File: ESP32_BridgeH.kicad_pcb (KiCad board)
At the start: 2 copper layers, 84.2 x 43.9 mm, 25 parts, among them J1 MT1, J2 MT2, J3 boot, J4 Serial, SW1 reset, U1 TB6612FNG, U2 ESP32-WROOM, U3 MPU6050, U4 LM7805_TO220

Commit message: Lodo added v2.0
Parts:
- added G***: LOGO, JuanDa_Lib:logoWolf, B.Cu at (188.9, 111.3)
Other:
- board text added: "ESP32 Wrober H-Bridge MPU6050 Serial Comunication"

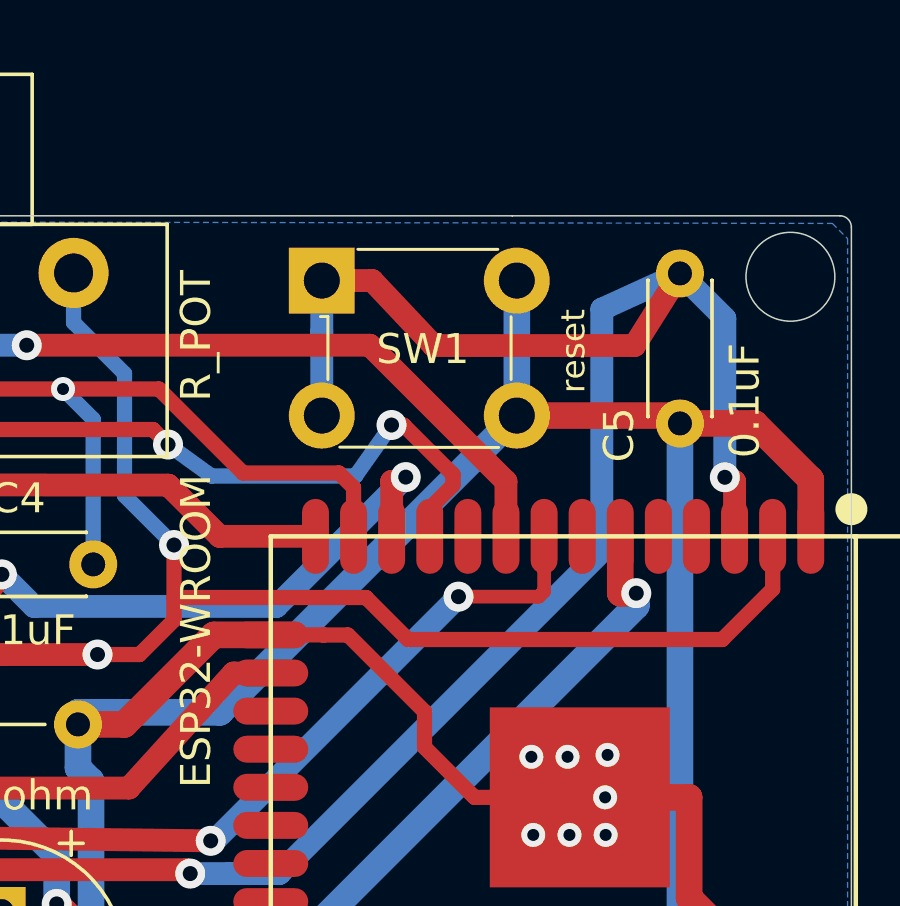
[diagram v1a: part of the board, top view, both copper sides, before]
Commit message: fix button problem
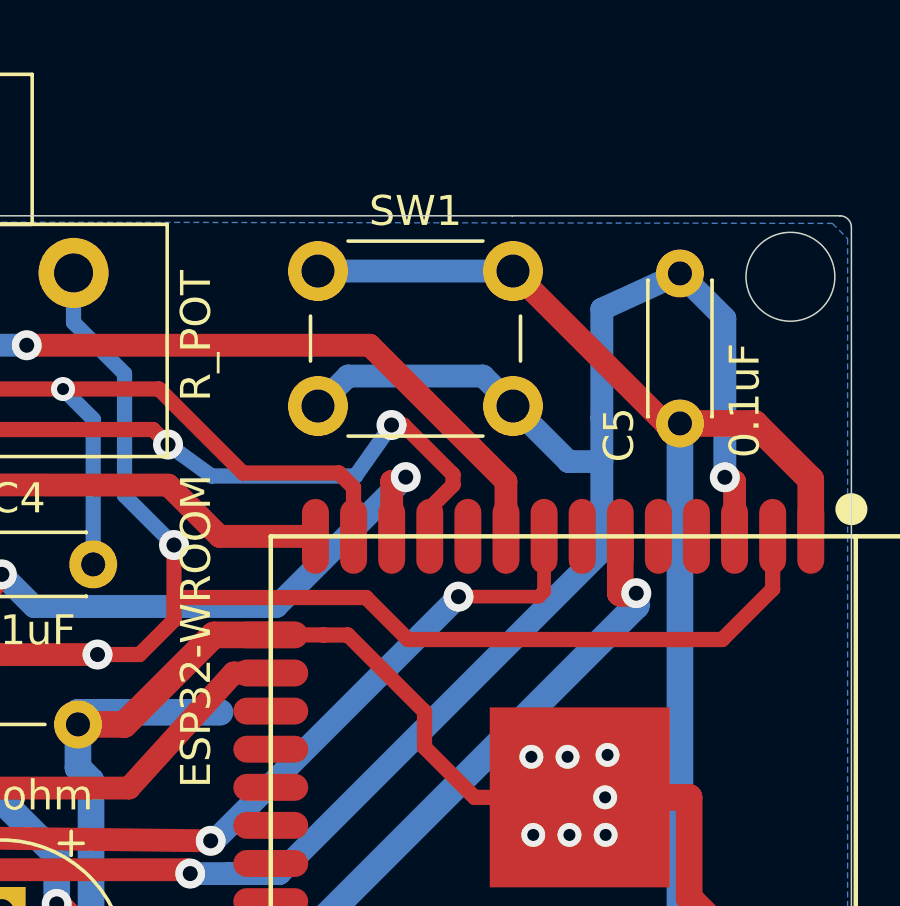
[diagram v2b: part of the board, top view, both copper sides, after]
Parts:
- SW1: value reset -> Reset; footprint digikey-footprints:Switch_Tactile_THT_6x6mm -> Button_Switch_THT:SW_PUSH_6mm
- moved SW1 0.34 mm to (188.8, 95.6)
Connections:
- SW1 pad 1: /reset -> GND
- SW1 pad 2: GND -> /reset
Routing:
- net GND: track 174.5 -> 164.6 mm
- net /reset: track 94.3 -> 86.7 mm
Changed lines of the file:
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@@
   )
   (setup
-    (last_trace_width 0.25)
+    (last_trace_width 0.762)
     (user_trace_width 0.508)
     (user_trace_width 0.762)
@@
     )
   )
-  (module digikey-footprints:Switch_Tactile_THT_6x6mm (layer F.Cu)
-    (at 188.976 95.885)
-    (descr http://www.te.com/commerce/DocumentDelivery/DDEController?Action=srchrtrv&DocNm=1825910&DocType=Customer+Drawing&DocLang=English)
-    (fp_text reference SW1 (at 3.3655 2.286 180) (layer F.SilkS)
-      (effects (font (size 1 1) (thickness 0.15)))
-    )
-    (fp_text value reset (at 8.382 2.3495 90) (layer F.SilkS)
-      (effects (font (size 0.8 0.8) (thickness 0.15)))
-    )
-    (fp_line (start 0.2032 1.2004) (end -0.0468 1.2004) (layer F.SilkS) (width 0.1))
-    (fp_line (start 5.8928 5.5626) (end 0.6 5.5528) (layer F.SilkS) (width 0.1))
-    (fp_line (start 6.3092 1.2048) (end 6.3092 3.3) (layer F.SilkS) (width 0.1))
-    (fp_line (start 0.2032 1.1938) (end 0.2032 3.302) (layer F.SilkS) (width 0.1))
-    (fp_line (start 1.2 -1.0414) (end 5.8674 -1.0414) (layer F.SilkS) (width 0.1))
-    (fp_line (start -1.35 -1.35) (end -1.35 5.85) (layer F.CrtYd) (width 0.05))
-    (fp_line (start 7.85 -1.35) (end -1.35 -1.35) (layer F.CrtYd) (width 0.05))
-    (fp_line (start 7.85 5.85) (end -1.35 5.85) (layer F.CrtYd) (width 0.05))
-    (fp_line (start 7.85 -1.35) (end 7.85 5.85) (layer F.CrtYd) (width 0.05))
-    (fp_text user %R (at 3.3782 2.286) (layer F.Fab)
-      (effects (font (size 1 1) (thickness 0.15)))
-    )
-    (fp_line (start 0.25 -1) (end 0.25 5.5) (layer F.Fab) (width 0.1))
-    (fp_line (start 6.25 5.5) (end 0.25 5.5) (layer F.Fab) (width 0.1))
-    (fp_line (start 6.25 -1) (end 6.25 5.5) (layer F.Fab) (width 0.1))
-    (fp_line (start 0.25 -1) (end 6.25 -1) (layer F.Fab) (width 0.1))
-    (pad 1 thru_hole rect (at 0 0) (size 2.2 2.2) (drill 1.2) (layers *.Cu *.Mask)
+  (module Button_Switch_THT:SW_PUSH_6mm (layer F.Cu)
+    (at 188.849 95.5675)
+    (descr https://www.omron.com/ecb/products/pdf/en-b3f.pdf)
+    (tags "tact sw push 6mm")
+    (fp_text reference SW1 (at 3.25 -2) (layer F.SilkS)
+      (effects (font (size 1 1) (thickness 0.15)))
+    )
+    (fp_text value Reset (at 3.75 6.7) (layer F.Fab)
+      (effects (font (size 1 1) (thickness 0.15)))
+    )
+    (fp_text user %R (at 3.25 2.25) (layer F.Fab)
+      (effects (font (size 1 1) (thickness 0.15)))
+    )
+    (fp_line (start 3.25 -0.75) (end 6.25 -0.75) (layer F.Fab) (width 0.1))
+    (fp_line (start 6.25 -0.75) (end 6.25 5.25) (layer F.Fab) (width 0.1))
+    (fp_line (start 6.25 5.25) (end 0.25 5.25) (layer F.Fab) (width 0.1))
+    (fp_line (start 0.25 5.25) (end 0.25 -0.75) (layer F.Fab) (width 0.1))
+    (fp_line (start 0.25 -0.75) (end 3.25 -0.75) (layer F.Fab) (width 0.1))
+    (fp_line (start 7.75 6) (end 8 6) (layer F.CrtYd) (width 0.05))
+    (fp_line (start 8 6) (end 8 5.75) (layer F.CrtYd) (width 0.05))
+    (fp_line (start 7.75 -1.5) (end 8 -1.5) (layer F.CrtYd) (width 0.05))
+    (fp_line (start 8 -1.5) (end 8 -1.25) (layer F.CrtYd) (width 0.05))
+    (fp_line (start -1.5 -1.25) (end -1.5 -1.5) (layer F.CrtYd) (width 0.05))
+    (fp_line (start -1.5 -1.5) (end -1.25 -1.5) (layer F.CrtYd) (width 0.05))
+    (fp_line (start -1.5 5.75) (end -1.5 6) (layer F.CrtYd) (width 0.05))
+    (fp_line (start -1.5 6) (end -1.25 6) (layer F.CrtYd) (width 0.05))
+    (fp_line (start -1.25 -1.5) (end 7.75 -1.5) (layer F.CrtYd) (width 0.05))
+    (fp_line (start -1.5 5.75) (end -1.5 -1.25) (layer F.CrtYd) (width 0.05))
+    (fp_line (start 7.75 6) (end -1.25 6) (layer F.CrtYd) (width 0.05))
+    (fp_line (start 8 -1.25) (end 8 5.75) (layer F.CrtYd) (width 0.05))
+    (fp_line (start 1 5.5) (end 5.5 5.5) (layer F.SilkS) (width 0.12))
+    (fp_line (start -0.25 1.5) (end -0.25 3) (layer F.SilkS) (width 0.12))
+    (fp_line (start 5.5 -1) (end 1 -1) (layer F.SilkS) (width 0.12))
+    (fp_line (start 6.75 3) (end 6.75 1.5) (layer F.SilkS) (width 0.12))
+    (fp_circle (center 3.25 2.25) (end 1.25 2.5) (layer F.Fab) (width 0.1))
+    (pad 2 thru_hole circle (at 0 4.5 90) (size 2 2) (drill 1.1) (layers *.Cu *.Mask)
       (net 2 /reset))
-    (pad 2 thru_hole circle (at 6.5 0) (size 2.2 2.2) (drill 1.2) (layers *.Cu *.Mask)
-      (net 1 GND))
-    (pad 4 thru_hole circle (at 6.5 4.5) (size 2.2 2.2) (drill 1.2) (layers *.Cu *.Mask)
+    (pad 1 thru_hole circle (at 0 0 90) (size 2 2) (drill 1.1) (layers *.Cu *.Mask)
       (net 1 GND))
-    (pad 3 thru_hole circle (at 0 4.5) (size 2.2 2.2) (drill 1.2) (layers *.Cu *.Mask)
+    (pad 2 thru_hole circle (at 6.5 4.5 90) (size 2 2) (drill 1.1) (layers *.Cu *.Mask)
       (net 2 /reset))
+    (pad 1 thru_hole circle (at 6.5 0 90) (size 2 2) (drill 1.1) (layers *.Cu *.Mask)
+      (net 1 GND))
     (model ${KISYS3DMOD}/Button_Switch_THT.3dshapes/SW_PUSH_6mm.wrl
       (at (xyz 0 0 0))
@@
   (segment (start 199.3974 113.111) (end 198.42 113.111) (width 0.889) (layer F.Cu) (net 1))
   (segment (start 199.3974 113.111) (end 201.2198 113.111) (width 0.889) (layer F.Cu) (net 1))
-  (segment (start 195.476 100.385) (end 185.5845 110.2765) (width 0.889) (layer B.Cu) (net 1))
   (segment (start 185.5845 110.2765) (end 180.848 110.2765) (width 0.889) (layer B.Cu) (net 1))
   (segment (start 180.848 110.68) (end 180.848 110.2765) (width 0.889) (layer B.Cu) (net 1))
-  (segment (start 195.476 100.385) (end 195.476 95.885) (width 0.889) (layer B.Cu) (net 1))
   (segment (start 205.275 122.411) (end 205.275 120.5162) (width 0.889) (layer F.Cu) (net 1))
   (segment (start 205.275 120.5162) (end 201.2198 116.461) (width 0.889) (layer F.Cu) (net 1))
@@
   (segment (start 200.914 100.648) (end 203.4068 100.648) (width 0.889) (layer F.Cu) (net 1))
   (segment (start 203.4068 100.648) (end 205.275 102.5162) (width 0.889) (layer F.Cu) (net 1))
-  (segment (start 195.476 100.385) (end 200.651 100.385) (width 0.889) (layer F.Cu) (net 1))
-  (segment (start 200.651 100.385) (end 200.914 100.648) (width 0.889) (layer F.Cu) (net 1))
   (segment (start 205.275 104.411) (end 205.275 102.5162) (width 0.889) (layer F.Cu) (net 1))
   (segment (start 198.42 113.111) (end 197.575 113.111) (width 0.889) (layer F.Cu) (net 1))
@@
   (segment (start 146.812 109.012) (end 146.812 107.252) (width 1.016) (layer F.Cu) (net 1))
   (segment (start 148.95 111.15) (end 146.812 109.012) (width 1.016) (layer F.Cu) (net 1))
+  (segment (start 200.4295 100.648) (end 200.914 100.648) (width 0.762) (layer F.Cu) (net 1))
+  (segment (start 195.349 95.5675) (end 200.4295 100.648) (width 0.762) (layer F.Cu) (net 1))
+  (segment (start 188.849 95.5675) (end 195.349 95.5675) (width 0.762) (layer B.Cu) (net 1))
   (segment (start 169.746 118.872) (end 173.6781 118.872) (width 0.762) (layer F.Cu) (net 2))
   (segment (start 173.6781 118.872) (end 177.0274 115.5227) (width 0.762) (layer F.Cu) (net 2))
   (segment (start 177.0274 115.5227) (end 184.4606 115.5227) (width 0.762) (layer F.Cu) (net 2))
   (segment (start 184.4606 115.5227) (end 184.5897 115.6518) (width 0.762) (layer F.Cu) (net 2))
-  (segment (start 188.976 95.885) (end 188.976 97.5663) (width 0.762) (layer B.Cu) (net 2))
-  (segment (start 188.976 100.385) (end 188.976 97.5663) (width 0.762) (layer B.Cu) (net 2))
   (segment (start 202.4106 102.4421) (end 202.5482 102.5797) (width 0.762) (layer F.Cu) (net 2))
   (segment (start 202.5482 102.5797) (end 202.735 102.5797) (width 0.762) (layer F.Cu) (net 2))
@@
   (segment (start 198.3105 104.902) (end 187.5607 115.6518) (width 0.762) (layer B.Cu) (net 2))
   (segment (start 187.5607 115.6518) (end 185.8992 115.6518) (width 0.762) (layer B.Cu) (net 2))
-  (segment (start 198.3105 96.8375) (end 198.3105 104.902) (width 0.762) (layer B.Cu) (net 2))
   (segment (start 200.914 95.648) (end 198.3105 96.8375) (width 0.762) (layer B.Cu) (net 2))
   (segment (start 155.93 126.81) (end 158.35 124.39) (width 0.762) (layer B.Cu) (net 2))
@@
   (segment (start 160.578 118.872) (end 169.746 118.872) (width 0.762) (layer B.Cu) (net 2))
   (segment (start 158.35 121.1) (end 160.578 118.872) (width 0.762) (layer B.Cu) (net 2))
-  (segment (start 190.6573 95.885) (end 188.976 95.885) (width 0.762) (layer F.Cu) (net 2))
-  (segment (start 192.7 98.05) (end 190.6573 95.885) (width 0.762) (layer F.Cu) (net 2))
-  (segment (start 200.914 95.648) (end 199.4 98.05) (width 0.762) (layer F.Cu) (net 2))
-  (segment (start 199.4 98.05) (end 192.7 98.05) (width 0.762) (layer F.Cu) (net 2))
+  (segment (start 198.3105 96.8375) (end 198.3105 100.457) (width 0.762) (layer B.Cu) (net 2))
+  (segment (start 197.199 101.9175) (end 198.3105 101.9175) (width 0.762) (layer B.Cu) (net 2))
+  (segment (start 195.349 100.0675) (end 197.199 101.9175) (width 0.762) (layer B.Cu) (net 2))
+  (segment (start 198.3105 101.9175) (end 198.3105 104.902) (width 0.762) (layer B.Cu) (net 2))
+  (segment (start 198.3105 100.457) (end 198.3105 101.9175) (width 0.762) (layer B.Cu) (net 2))
+  (segment (start 189.848999 99.067501) (end 194.349001 99.067501) (width 0.762) (layer B.Cu) (net 2))
+  (segment (start 194.349001 99.067501) (end 195.349 100.0675) (width 0.762) (layer B.Cu) (net 2))
+  (segment (start 188.849 100.0675) (end 189.848999 99.067501) (width 0.762) (layer B.Cu) (net 2))
   (segment (start 169.746 111.252) (end 163.3948 111.252) (width 0.762) (layer F.Cu) (net 3))
   (segment (start 163.3948 111.252) (end 161.0088 108.866) (width 0.762) (layer F.Cu) (net 3))
